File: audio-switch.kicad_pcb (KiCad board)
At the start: 2 copper layers, 21 parts, among them J1 AudioJack4_Out, J2 AudioJack4_Out, J3 AudioJack4_IN, J4 AudioJack4_IN, J5 AudioJack4_IN, J6 AudioJack4_IN, U1 Pico, U2 CD4052B, U3 CD4052B

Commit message: Update
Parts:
- U2, U3: footprint CD4052BM:SOIC127P600X175-16N -> Package_DIP:DIP-16_W7.62mm_Socket
- moved J2 112.1 mm to (57.5, 56.5), turned to 180 degrees
- moved U2 108.5 mm to (100.5, 16.0)
- moved J1 104.7 mm to (49.0, 56.5), turned to 180 degrees
- moved J4 103.3 mm to (74.0, 27.0)
- moved U3 102.3 mm to (100.5, 37.5)
- moved J5 100.1 mm to (82.5, 27.0)
- moved J3 96.5 mm to (65.5, 27.0)
- moved U1 93.5 mm to (124.5, 40.5)
- moved J6 93.3 mm to (91.0, 27.0)
- moved R2 74.0 mm to (106.0, 66.0), turned to 90 degrees
- moved R4 41.8 mm to (108.5, 66.0), turned to 90 degrees
- moved R3 41.2 mm to (108.5, 60.5), turned to 90 degrees
- moved R1 39.8 mm to (106.0, 60.5), turned to 90 degrees
- moved D1 22.9 mm to (100.5, 60.5), turned to 270 degrees
- moved D2 15.7 mm to (100.5, 66.0), turned to 270 degrees
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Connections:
- net Net-(U1-Pad33) renamed GNDA
- net Net-(U1-Pad37) renamed +3V3
- U1 pad 13: Net-(U1-Pad13) -> GND
- U1 pad 18: Net-(U1-Pad18) -> GND
- U1 pad 23: Net-(U1-Pad23) -> GND
- U1 pad 28: Net-(U1-Pad28) -> GND
- U1 pad 3: Net-(U1-Pad3) -> GND
- U1 pad 38: Net-(U1-Pad38) -> GND
- U1 pad 40: Net-(U1-Pad40) -> +5V
- U1 pad 8: Net-(U1-Pad8) -> GND
- U2 pad 7: Net-(U2-Pad7) -> +5V
- U2 pad 8: Net-(U2-Pad8) -> GND
- U3 pad 7: Net-(U3-Pad7) -> +5V
- U3 pad 8: Net-(U3-Pad8) -> GND

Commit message: Updated pico code and moved some stuff around
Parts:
- J1: value AudioJack4_Out -> OUT_1
- renumbered J3 to IN_1, J4 to IN_2, J5 to IN_3, J6 to IN_4, J2 to OUT_2

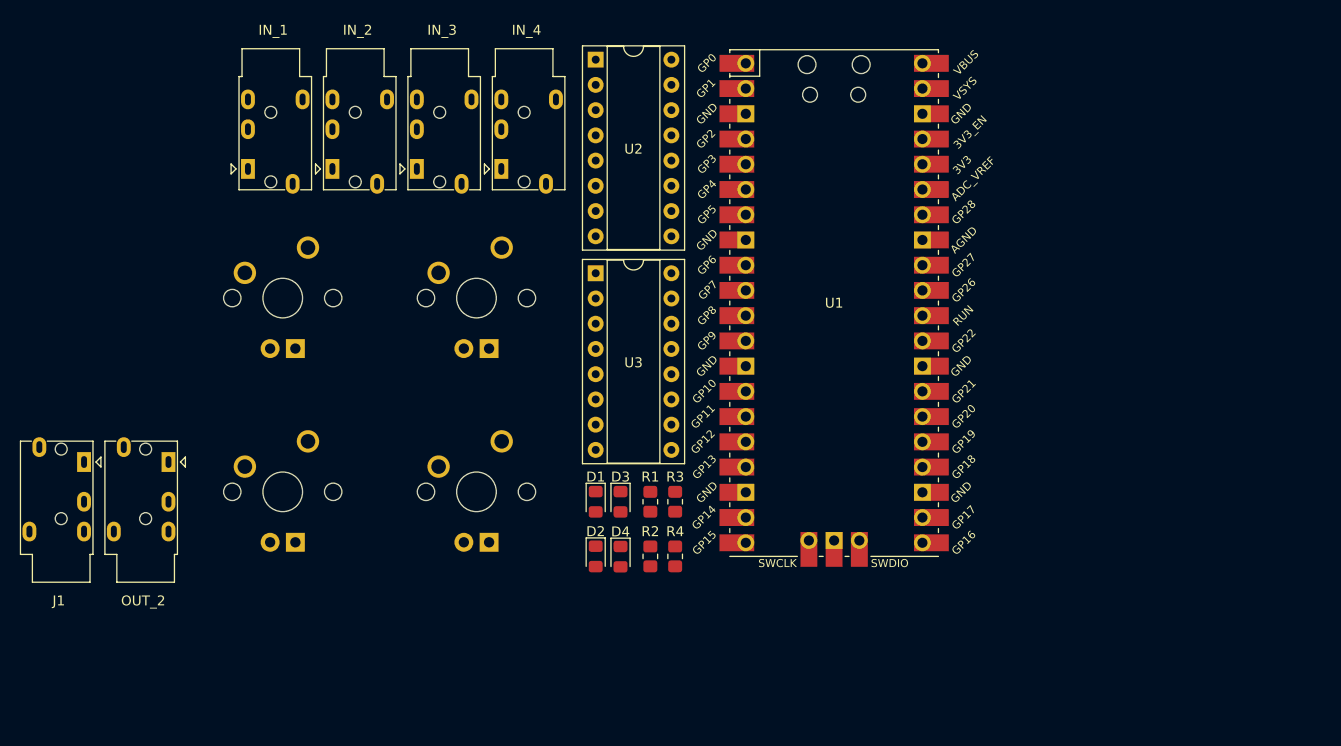
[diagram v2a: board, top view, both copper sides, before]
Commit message: Remove pico and use sr latch for input slection
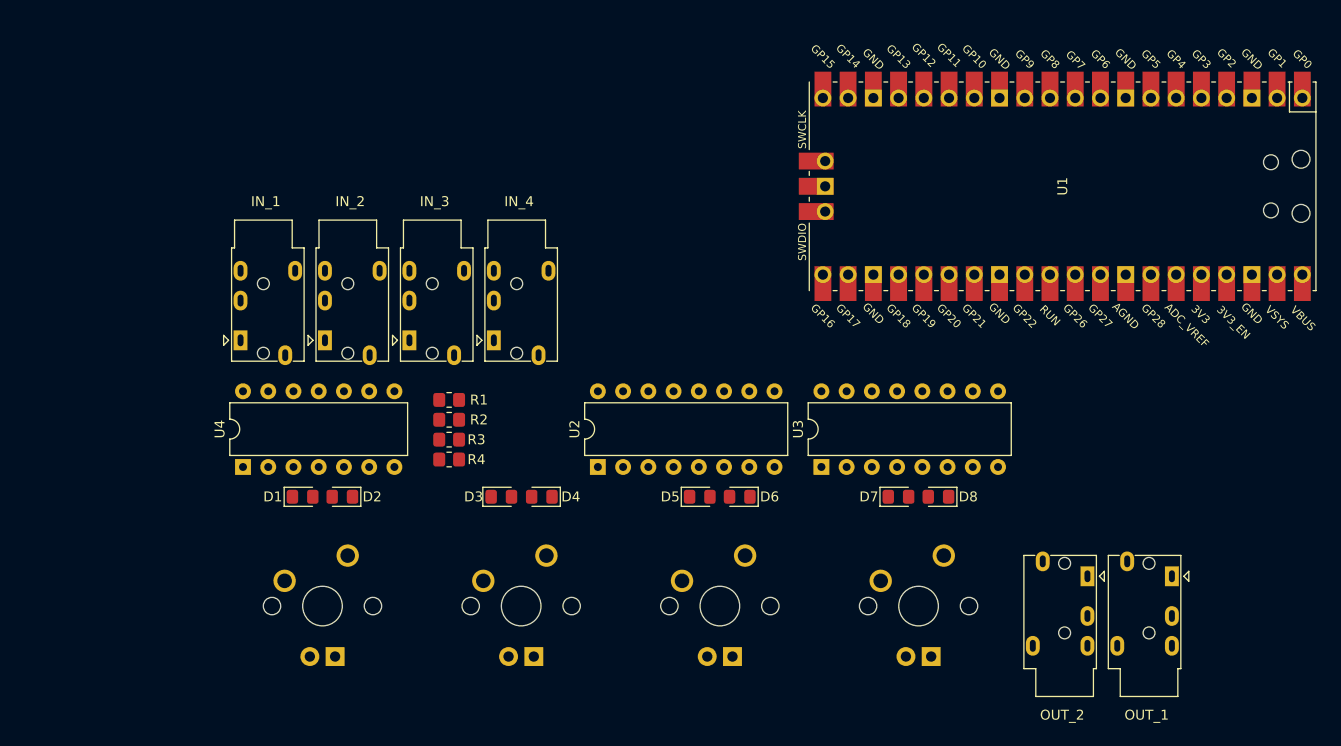
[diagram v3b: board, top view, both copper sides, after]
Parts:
- removed J1: OUT_1, Connector_Audio:Jack_3.5mm_PJ320E_Horizontal
- added D5: D_Small, Diode_SMD:D_0805_2012Metric_Pad1.15x1.40mm_HandSolder, F.Cu at (111.0, 60.0)
- added D6: D_Small, Diode_SMD:D_0805_2012Metric_Pad1.15x1.40mm_HandSolder, F.Cu at (115.0, 60.0)
- added D7: D_Small, Diode_SMD:D_0805_2012Metric_Pad1.15x1.40mm_HandSolder, F.Cu at (131.0, 60.0)
- added D8: D_Small, Diode_SMD:D_0805_2012Metric_Pad1.15x1.40mm_HandSolder, F.Cu at (135.0, 60.0)
- added OUT_1: OUT_1, Connector_Audio:Jack_3.5mm_PJ320E_Horizontal, F.Cu at (158.5, 68.0)
- added U4: 7402, Package_DIP:DIP-14_W7.62mm, F.Cu at (65.0, 57.0)
- MX1, MX2, MX3, MX4: value MX-LED -> MX-NoLED
- OUT_2: value AudioJack4_Out -> OUT_2
- R1, R2, R3, R4: value R_Led -> R_Small
- U2, U3: footprint Package_DIP:DIP-16_W7.62mm_Socket -> Package_DIP:DIP-16_W7.62mm
- moved OUT_2 93.2 mm to (150.0, 68.0)
- moved MX4 46.0 mm to (133.0, 71.0)
- moved U2 41.0 mm to (100.7, 57.0), turned to 90 degrees
- moved MX3 39.5 mm to (113.0, 71.0)
- moved MX1 31.3 mm to (73.0, 71.0)
- moved U3 29.9 mm to (123.2, 57.0), turned to 90 degrees
- moved D1 29.5 mm to (71.0, 60.0), turned to 0 degrees
- moved MX2 26.6 mm to (93.0, 71.0)
- moved D2 26.2 mm to (75.0, 60.0), turned to 180 degrees
- moved U1 25.8 mm to (147.5, 28.8), turned to 270 degrees
- moved R4 24.8 mm to (85.8, 56.2), turned to 0 degrees
- moved R2 24.5 mm to (85.8, 52.2), turned to 0 degrees
- moved R3 23.6 mm to (85.8, 54.2), turned to 0 degrees
- moved R1 22.7 mm to (85.8, 50.2), turned to 0 degrees
- moved IN_1 17.3 mm to (64.8, 44.2)
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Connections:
- D1 pad 1: Row0 -> Net-(D1-Pad1)
- D2 pad 1: Row1 -> Net-(D2-Pad1)
- D2 pad 2: Net-(D2-Pad2) -> Net-(D1-Pad2)
- D3 pad 1: Row0 -> Net-(D2-Pad1)
- D4 pad 1: Row1 -> Net-(D4-Pad1)
- D4 pad 2: Net-(D4-Pad2) -> Net-(D3-Pad2)
- MX1 pad 1: Col0 -> +5V
- MX1 pad 3: Net-(MX1-Pad3) -> (no net)
- MX1 pad 4: LEDRow0 -> (no net)
- MX2 pad 1: Col0 -> +5V
- MX2 pad 2: Net-(D2-Pad2) -> Net-(D3-Pad2)
- MX2 pad 3: Net-(MX2-Pad3) -> (no net)
- MX2 pad 4: LEDRow1 -> (no net)
- MX3 pad 1: Col1 -> +5V
- MX3 pad 2: Net-(D3-Pad2) -> Net-(D5-Pad2)
- MX3 pad 3: Net-(MX3-Pad3) -> (no net)
- MX3 pad 4: LEDRow0 -> (no net)
- MX4 pad 1: Col1 -> +5V
- MX4 pad 2: Net-(D4-Pad2) -> Net-(D7-Pad2)
- MX4 pad 3: Net-(MX4-Pad3) -> (no net)
- MX4 pad 4: LEDRow1 -> (no net)
- R1 pad 1: Net-(MX1-Pad3) -> Net-(D1-Pad1)
- R1 pad 2: LEDCol0 -> GND
- R2 pad 1: Net-(MX2-Pad3) -> Net-(D4-Pad1)
- R2 pad 2: LEDCol0 -> GND
- R3 pad 1: Net-(MX3-Pad3) -> Net-(D2-Pad1)
- R3 pad 2: LEDCol1 -> GND
- R4 pad 1: Net-(MX4-Pad3) -> Net-(D5-Pad1)
- R4 pad 2: LEDCol1 -> GND
- U1 pad 1: LEDRow0 -> Net-(U1-Pad1)
- U1 pad 10: Col1 -> Net-(U1-Pad10)
- U1 pad 19: Select_A -> Net-(U1-Pad19)
- U1 pad 2: LEDRow1 -> Net-(U1-Pad2)
- U1 pad 20: Select_B -> Net-(U1-Pad20)
- U1 pad 4: LEDCol0 -> Net-(U1-Pad4)
- U1 pad 5: LEDCol1 -> Net-(U1-Pad5)
- U1 pad 6: Row0 -> Net-(U1-Pad6)
- U1 pad 7: Row1 -> Net-(U1-Pad7)
- U1 pad 9: Col0 -> Net-(U1-Pad9)
- U2 pad 7: +5V -> GND
- U3 pad 7: +5V -> GND

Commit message: Added amps
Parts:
- removed D1, D2, D3, D4, D5, D6, D7, D8: D_Small, Diode_SMD:D_0805_2012Metric_Pad1.15x1.40mm_HandSolder
- removed IN_1, IN_2, IN_3, IN_4: AudioJack4_IN, Connector_Audio:Jack_3.5mm_PJ320E_Horizontal
- removed MX1, MX2, MX3, MX4: MX-NoLED, MX_Only:MXOnly-1U
- removed OUT_1: OUT_1, Connector_Audio:Jack_3.5mm_PJ320E_Horizontal
- removed OUT_2: OUT_2, Connector_Audio:Jack_3.5mm_PJ320E_Horizontal
- removed R1, R2, R3, R4: R_Small, Resistor_SMD:R_0805_2012Metric_Pad1.20x1.40mm_HandSolder
- removed U1: Pico, pi:RPi_Pico_SMD_TH
- removed U2, U3: CD4052B, Package_DIP:DIP-16_W7.62mm
- removed U4: 7402, Package_DIP:DIP-14_W7.62mm

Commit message: Latch
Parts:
- added BASS1: 10k, Potentiometer_THT:Potentiometer_Alps_RK09L_Double_Vertical, F.Cu at (122.5, 84.2)
- added C1: 0.1u, Capacitor_SMD:C_0805_2012Metric_Pad1.18x1.45mm_HandSolder, F.Cu at (-24.1, 164.8)
- added C10: 0.1u, Capacitor_SMD:C_0805_2012Metric_Pad1.18x1.45mm_HandSolder, F.Cu at (-15.5, 138.2)
- added C11: 100u, Capacitor_SMD:C_0805_2012Metric_Pad1.18x1.45mm_HandSolder, F.Cu at (-21.8, 154.1)
- added C12: 0.1u, Capacitor_SMD:C_0805_2012Metric_Pad1.18x1.45mm_HandSolder, F.Cu at (-10.7, 138.2)
- added C13: 470p, Capacitor_SMD:C_0805_2012Metric_Pad1.18x1.45mm_HandSolder, F.Cu at (-16.8, 150.3)
- added C14: 10u, Capacitor_SMD:C_0805_2012Metric_Pad1.18x1.45mm_HandSolder, F.Cu at (-16.8, 147.3)
- added C15: 10u, Capacitor_SMD:C_0805_2012Metric_Pad1.18x1.45mm_HandSolder, F.Cu at (-7.19, 141.2)
- added C16: 0.033u, Capacitor_SMD:C_0805_2012Metric_Pad1.18x1.45mm_HandSolder, F.Cu at (-12.0, 141.2)
- added C17: 0.1u, Capacitor_SMD:C_0805_2012Metric_Pad1.18x1.45mm_HandSolder, F.Cu at (-25.1, 136.7)
- added C18: 1000u, Capacitor_SMD:C_0805_2012Metric_Pad1.18x1.45mm_HandSolder, F.Cu at (-20.3, 136.7)
- added C2: 100u, Capacitor_SMD:C_0805_2012Metric_Pad1.18x1.45mm_HandSolder, F.Cu at (-21.8, 157.1)
- added C3: 0.1u, Capacitor_SMD:C_0805_2012Metric_Pad1.18x1.45mm_HandSolder, F.Cu at (-16.8, 144.2)
- added C4: 470p, Capacitor_SMD:C_0805_2012Metric_Pad1.18x1.45mm_HandSolder, F.Cu at (1.76, 133.4)
- added C5: 10u, Capacitor_SMD:C_0805_2012Metric_Pad1.18x1.45mm_HandSolder, F.Cu at (-20.9, 169.7)
- added C6: 10u, Capacitor_SMD:C_0805_2012Metric_Pad1.18x1.45mm_HandSolder, F.Cu at (-5.88, 138.2)
- added C7: 0.033u, Capacitor_SMD:C_0805_2012Metric_Pad1.18x1.45mm_HandSolder, F.Cu at (-16.8, 141.2)
- added C8: 0.1u, Capacitor_SMD:C_0805_2012Metric_Pad1.18x1.45mm_HandSolder, F.Cu at (-12.0, 144.2)
- added C9: 1000u, Capacitor_SMD:C_0805_2012Metric_Pad1.18x1.45mm_HandSolder, F.Cu at (-21.8, 151.1)
- added D1: D_Small, Diode_SMD:D_0805_2012Metric_Pad1.15x1.40mm_HandSolder, F.Cu at (-2.37, 141.3)
- added D2: D_Small, Diode_SMD:D_0805_2012Metric_Pad1.15x1.40mm_HandSolder, F.Cu at (-7.17, 144.3)
- added D3: D_Small, Diode_SMD:D_0805_2012Metric_Pad1.15x1.40mm_HandSolder, F.Cu at (-16.8, 153.3)
- added D4: D_Small, Diode_SMD:D_0805_2012Metric_Pad1.15x1.40mm_HandSolder, F.Cu at (-12.0, 147.3)
- added D5: D_Small, Diode_SMD:D_0805_2012Metric_Pad1.15x1.40mm_HandSolder, F.Cu at (1.77, 136.5)
- added D6: D_Small, Diode_SMD:D_0805_2012Metric_Pad1.15x1.40mm_HandSolder, F.Cu at (6.58, 133.4)
- added D7: D_Small, Diode_SMD:D_0805_2012Metric_Pad1.15x1.40mm_HandSolder, F.Cu at (-12.0, 150.3)
- added D8: D_Small, Diode_SMD:D_0805_2012Metric_Pad1.15x1.40mm_HandSolder, F.Cu at (-16.9, 163.2)
- added GAIN1: 10k, Potentiometer_THT:Potentiometer_Alps_RK09L_Double_Vertical, F.Cu at (140.0, 75.5)
- added IN_1: AudioJack4_IN, Connector_Audio:Jack_3.5mm_PJ320E_Horizontal, F.Cu at (39.0, 21.5)
- added IN_2: AudioJack4_IN, Connector_Audio:Jack_3.5mm_PJ320E_Horizontal, F.Cu at (47.5, 21.5)
- added IN_3: AudioJack4_IN, Connector_Audio:Jack_3.5mm_PJ320E_Horizontal, F.Cu at (56.0, 21.5)
- added IN_4: AudioJack4_IN, Connector_Audio:Jack_3.5mm_PJ320E_Horizontal, F.Cu at (64.5, 21.5)
- added MX1: MX-NoLED, MX_Only:MXOnly-1U-NoLED, F.Cu at (127.5, 12.5)
- added MX2: MX-NoLED, MX_Only:MXOnly-1U-NoLED, F.Cu at (127.5, 32.0)
- added MX3: MX-NoLED, MX_Only:MXOnly-1U-NoLED, F.Cu at (108.0, 12.5)
- added MX4: MX-NoLED, MX_Only:MXOnly-1U-NoLED, F.Cu at (108.0, 32.0)
- added OUT_1: OUT_1, Connector_Audio:Jack_3.5mm_PJ320E_Horizontal, F.Cu at (72.9, 21.5)
- added R1: 10k, Resistor_SMD:R_0805_2012Metric_Pad1.20x1.40mm_HandSolder, F.Cu at (28.5, 48.2)
- added R2: 10k, Resistor_SMD:R_0805_2012Metric_Pad1.20x1.40mm_HandSolder, F.Cu at (28.5, 46.1)
- added R3: 10k, Resistor_SMD:R_0805_2012Metric_Pad1.20x1.40mm_HandSolder, F.Cu at (34.1, 46.1)
- added R4: 10k, Resistor_SMD:R_0805_2012Metric_Pad1.20x1.40mm_HandSolder, F.Cu at (34.1, 48.2)
- added R5: 10k, Resistor_SMD:R_0805_2012Metric_Pad1.20x1.40mm_HandSolder, F.Cu at (-2.43, 144.2)
- added R6: 10, Resistor_SMD:R_0805_2012Metric_Pad1.20x1.40mm_HandSolder, F.Cu at (6.52, 136.4)
- added R7: 10k, Resistor_SMD:R_0805_2012Metric_Pad1.20x1.40mm_HandSolder, F.Cu at (-7.24, 150.2)
- added R8: 10, Resistor_SMD:R_0805_2012Metric_Pad1.20x1.40mm_HandSolder, F.Cu at (-16.8, 159.2)
- added U1: 7402, Package_DIP:DIP-14_W7.62mm, F.Cu at (27.5, 28.1)
- added U2: DG509A, Package_DIP:DIP-16_W7.62mm, F.Cu at (39.5, 28.1)
- added U3: DG509A, Package_DIP:DIP-16_W7.62mm, F.Cu at (50.0, 28.1)
- added U4: LM386, Package_DIP:DIP-8_W7.62mm, F.Cu at (97.9, 142.5)
- added U5: LM386, Package_DIP:DIP-8_W7.62mm, F.Cu at (87.9, 142.5)
- added VOL1: 10k, Potentiometer_THT:Potentiometer_Alps_RK09L_Double_Vertical, F.Cu at (140.2, 91.5)
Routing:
- net /a: track 0.00 -> 18.7 mm
- net /d: track 0.00 -> 16.2 mm
- net GND: track 0.00 -> 14.0 mm, vias 0 -> 1
- net Select_A: track 0.00 -> 11.3 mm
- net Net-(U1-Pad13): track 0.00 -> 11.3 mm
- net /b: track 0.00 -> 6.46 mm
- net /c: track 0.00 -> 2.80 mm
- net Select_B: track 0.00 -> 2.54 mm
- net Net-(U1-Pad3): track 0.00 -> 2.54 mm

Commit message: Temp
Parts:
- moved D3 179.9 mm to (126.0, 43.9), turned to 90 degrees
- moved D8 178.7 mm to (116.0, 43.9), turned to 90 degrees
- moved D7 176.9 mm to (129.3, 43.9), turned to 90 degrees
- moved D4 159.5 mm to (109.4, 43.9), turned to 90 degrees
- moved D1 158.5 mm to (122.7, 43.9), turned to 90 degrees
- moved D2 151.3 mm to (106.0, 43.9), turned to 90 degrees
- moved C5 150.7 mm to (128.8, 152.5)
- moved D5 149.7 mm to (119.4, 43.9), turned to 90 degrees
- moved D6 138.9 mm to (112.7, 43.9), turned to 90 degrees
- moved R7 106.4 mm to (98.2, 136.5)
- moved R6 30.4 mm to (-6.25, 164.0)
- moved U4 22.6 mm to (116.5, 155.2)
- moved U5 7.25 mm to (88.0, 135.2)
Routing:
- net Net-(D1-Pad2): track 0.00 -> 64.7 mm, vias 0 -> 2
- net Net-(D5-Pad2): track 0.00 -> 50.1 mm, vias 0 -> 2
- net Net-(D3-Pad2): track 0.00 -> 35.6 mm, vias 0 -> 2
- net Net-(D7-Pad2): track 0.00 -> 32.7 mm
- net /d: track 16.2 -> 19.5 mm
- net /b: track 6.46 -> 9.78 mm
- net /c: track 2.80 -> 6.12 mm
- net /a: track 18.7 -> 22.0 mm

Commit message: Board designed.
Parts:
- added H101: MountingHole_Pad, MountingHole:MountingHole_2.2mm_M2, F.Cu at (81.5, 53.5)
- added H102: MountingHole_Pad, MountingHole:MountingHole_2.2mm_M2, F.Cu at (176.0, 106.5)
- added H103: MountingHole_Pad, MountingHole:MountingHole_2.2mm_M2, F.Cu at (81.5, 106.5)
- added H104: MountingHole_Pad, MountingHole:MountingHole_2.2mm_M2, F.Cu at (176.0, 53.5)
- added J101: USB_C_Receptacle, Connector_USB:USB_C_Receptacle_Amphenol_12401610E4-2A, F.Cu at (172.0, 63.0)
- moved C9 169.4 mm to (136.0, 89.5), turned to 90 degrees
- moved R8 169.1 mm to (132.5, 80.0), turned to 90 degrees
- moved C17 166.1 mm to (132.5, 84.5), turned to 90 degrees
- moved R6 165.2 mm to (136.0, 80.0), turned to 90 degrees
- moved C18 160.0 mm to (132.5, 89.5), turned to 90 degrees
- moved C8 159.6 mm to (136.0, 84.5), turned to 90 degrees
- moved C13 152.0 mm to (118.0, 80.0), turned to 90 degrees
- moved C11 149.9 mm to (103.0, 71.0)
- moved C7 149.1 mm to (123.0, 89.5), turned to 90 degrees
- moved C2 146.3 mm to (96.5, 71.0)
- moved C1 144.8 mm to (99.2, 89.0)
- moved C16 141.3 mm to (119.5, 89.5), turned to 90 degrees
- moved C10 136.4 mm to (111.7, 89.1)
- moved C14 134.6 mm to (104.5, 89.0), turned to 90 degrees
- moved R1 134.3 mm to (162.2, 60.2), turned to 90 degrees
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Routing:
- net +5V: track 0.00 -> 303.9 mm, vias 0 -> 3
- net Net-(IN_1-PadR2): track 0.00 -> 73.7 mm, vias 0 -> 2
- net Net-(IN_1-PadS): track 0.00 -> 65.5 mm, vias 0 -> 2
- net Input_Right: track 0.00 -> 62.4 mm
- net Net-(IN_2-PadR2): track 0.00 -> 59.1 mm, vias 0 -> 1
- net Net-(C16-Pad2): track 0.00 -> 57.9 mm, vias 0 -> 2
- net Net-(IN_1-PadR1): track 0.00 -> 53.5 mm
- net Net-(IN_2-PadS): track 0.00 -> 53.1 mm, vias 0 -> 1
- net Input_Left: track 0.00 -> 49.5 mm
- net Net-(IN_2-PadR1): track 0.00 -> 45.0 mm
- net GND: track 14.0 -> 58.8 mm, vias 1 -> 14
- net Net-(IN_3-PadR2): track 0.00 -> 44.7 mm
- net Net-(IN_3-PadS): track 0.00 -> 41.9 mm
- net Net-(C7-Pad2): track 0.00 -> 40.9 mm, vias 0 -> 1
- net Net-(IN_1-PadT): track 0.00 -> 39.1 mm
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- added copper zone on B.Cu, net GND
- added copper zone on F.Cu, net GND
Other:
- board outline added: 99.5 x 58 mm
